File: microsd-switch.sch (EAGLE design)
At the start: 12 parts, among them IC1 SN74CBT3257D, IC2 SN74CBT3257D, U1 USD-SOCKETNEW

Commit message: Reduced uSD header connector size.
Signed-off-by: Joel Fernandes <joelf@ti.com>
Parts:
- JP2: value USD-HEADER-TARGET -> SD_HEADER_TARGET; device SparkFun:M08LOCK -> joels-parts:M08
- JP3: value USD-HEADER-HOST -> SD_HEADER_HOST; device SparkFun:M08LOCK -> joels-parts:M08
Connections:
- net CLK-A: now also JP2.6; no longer JP2.3
- net CLK-B: now also JP3.6; no longer JP3.3
- net CMD-A: now also JP2.3; no longer JP2.6
- net CMD-B: now also JP3.3; no longer JP3.6
- net DAT0-A: now also JP2.7; no longer JP2.2
- net DAT0-B: now also JP3.7; no longer JP3.2
- net DAT1-A: now also JP2.8; no longer JP2.1
- net DAT1-B: now also JP3.8; no longer JP3.1
- net DAT2-A: now also JP2.1; no longer JP2.8
- net DAT2-B: now also JP3.1; no longer JP3.8
- net DAT3-A: now also JP2.2; no longer JP2.7
- net DAT3-B: now also JP3.2; no longer JP3.7
- net GND: now also JP2.4, JP3.4; no longer JP2.5, JP3.5
- net VDD-A: now also JP2.5; no longer JP2.4
- net VDD-B: now also JP3.5; no longer JP3.4
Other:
- moved on the sheet: JP2, JP3
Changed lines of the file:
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@@
 <part name="GND2" library="supply1" deviceset="GND" device=""/>
 <part name="P+1" library="supply1" deviceset="VCC" device=""/>
-<part name="JP2" library="SparkFun" deviceset="M08" device="LOCK" value="USD-HEADER-TARGET"/>
-<part name="JP3" library="SparkFun" deviceset="M08" device="LOCK" value="USD-HEADER-HOST"/>
 <part name="IC1" library="joels-parts" deviceset="SN74CBT3257" device="D"/>
 <part name="IC2" library="joels-parts" deviceset="SN74CBT3257" device="D"/>
@@
 <part name="LED2" library="led" deviceset="LED" device="CHIP-LED0805" value="SWITCH"/>
 <part name="GND1" library="supply1" deviceset="GND" device=""/>
+<part name="JP2" library="joels-parts" deviceset="M08" device="" value="SD_HEADER_TARGET"/>
+<part name="JP3" library="joels-parts" deviceset="M08" device="" value="SD_HEADER_HOST"/>
 </parts>
 <sheets>
@@
 <instance part="GND2" gate="1" x="17.78" y="0"/>
 <instance part="P+1" gate="VCC" x="-15.24" y="2.54" rot="MR0"/>
-<instance part="JP2" gate="G$1" x="-7.62" y="71.12" rot="MR180"/>
-<instance part="JP3" gate="G$1" x="-7.62" y="35.56" rot="MR180"/>
 <instance part="IC1" gate="A" x="45.72" y="60.96"/>
 <instance part="IC2" gate="A" x="45.72" y="22.86"/>
@@
 <instance part="LED2" gate="G$1" x="43.18" y="-7.62" rot="R90"/>
 <instance part="GND1" gate="1" x="63.5" y="-12.7"/>
+<instance part="JP2" gate="G$1" x="-7.62" y="68.58"/>
+<instance part="JP3" gate="G$1" x="-7.62" y="33.02"/>
 </instances>
 <busses>
@@
 <wire x1="-2.54" y1="78.74" x2="12.7" y2="78.74" width="0.1524" layer="91"/>
 <label x="2.54" y="78.74" size="1.778" layer="95"/>
-<pinref part="JP2" gate="G$1" pin="1"/>
+<pinref part="JP2" gate="G$1" pin="8"/>
 </segment>
 <segment>
@@
 <wire x1="-2.54" y1="76.2" x2="12.7" y2="76.2" width="0.1524" layer="91"/>
 <label x="2.54" y="76.2" size="1.778" layer="95"/>
-<pinref part="JP2" gate="G$1" pin="2"/>
+<pinref part="JP2" gate="G$1" pin="7"/>
 </segment>
 <segment>
@@
 </segment>
 <segment>
-<pinref part="JP2" gate="G$1" pin="4"/>
 <wire x1="-2.54" y1="71.12" x2="12.7" y2="71.12" width="0.1524" layer="91"/>
 <label x="2.54" y="71.12" size="1.778" layer="95"/>
+<pinref part="JP2" gate="G$1" pin="5"/>
 </segment>
 </net>
@@
 </segment>
 <segment>
-<pinref part="JP2" gate="G$1" pin="6"/>
 <wire x1="-2.54" y1="66.04" x2="12.7" y2="66.04" width="0.1524" layer="91"/>
 <label x="2.54" y="66.04" size="1.778" layer="95"/>
+<pinref part="JP2" gate="G$1" pin="3"/>
 </segment>
 </net>
@@
 <wire x1="-2.54" y1="63.5" x2="12.7" y2="63.5" width="0.1524" layer="91"/>
 <label x="5.08" y="63.5" size="1.778" layer="95"/>
-<pinref part="JP2" gate="G$1" pin="7"/>
+<pinref part="JP2" gate="G$1" pin="2"/>
 </segment>
 <segment>
@@
 <wire x1="-2.54" y1="60.96" x2="12.7" y2="60.96" width="0.1524" layer="91"/>
 <label x="5.08" y="60.96" size="1.778" layer="95"/>
-<pinref part="JP2" gate="G$1" pin="8"/>
+<pinref part="JP2" gate="G$1" pin="1"/>
 </segment>
 <segment>
@@
 <wire x1="-2.54" y1="43.18" x2="7.62" y2="43.18" width="0.1524" layer="91"/>
 <label x="5.08" y="43.18" size="1.778" layer="95"/>
-<pinref part="JP3" gate="G$1" pin="1"/>
+<pinref part="JP3" gate="G$1" pin="8"/>
 </segment>
 <segment>
@@
 <wire x1="-2.54" y1="40.64" x2="7.62" y2="40.64" width="0.1524" layer="91"/>
 <label x="5.08" y="40.64" size="1.778" layer="95"/>
-<pinref part="JP3" gate="G$1" pin="2"/>
+<pinref part="JP3" gate="G$1" pin="7"/>
 </segment>
 <segment>
@@
 </segment>
 <segment>
-<pinref part="JP3" gate="G$1" pin="3"/>
 <wire x1="-2.54" y1="38.1" x2="7.62" y2="38.1" width="0.1524" layer="91"/>
 <label x="5.08" y="38.1" size="1.778" layer="95"/>
+<pinref part="JP3" gate="G$1" pin="6"/>
 </segment>
 </net>
@@
 </segment>
 <segment>
-<pinref part="JP3" gate="G$1" pin="6"/>
 <wire x1="-2.54" y1="30.48" x2="7.62" y2="30.48" width="0.1524" layer="91"/>
 <label x="5.08" y="30.48" size="1.778" layer="95"/>
+<pinref part="JP3" gate="G$1" pin="3"/>
 </segment>
 </net>
@@
 <wire x1="-2.54" y1="27.94" x2="7.62" y2="27.94" width="0.1524" layer="91"/>
 <label x="5.08" y="27.94" size="1.778" layer="95"/>
-<pinref part="JP3" gate="G$1" pin="7"/>
+<pinref part="JP3" gate="G$1" pin="2"/>
 </segment>
 <segment>
@@
 <wire x1="-2.54" y1="25.4" x2="7.62" y2="25.4" width="0.1524" layer="91"/>
 <label x="5.08" y="25.4" size="1.778" layer="95"/>
-<pinref part="JP3" gate="G$1" pin="8"/>
+<pinref part="JP3" gate="G$1" pin="1"/>
 </segment>
 <segment>
@@
 </segment>
 <segment>
-<pinref part="JP3" gate="G$1" pin="4"/>
 <wire x1="-2.54" y1="35.56" x2="7.62" y2="35.56" width="0.1524" layer="91"/>
 <label x="5.08" y="35.56" size="1.778" layer="95"/>
+<pinref part="JP3" gate="G$1" pin="5"/>
 </segment>
 </net>
@@
 </segment>
 <segment>
-<pinref part="JP3" gate="G$1" pin="5"/>
 <wire x1="-2.54" y1="33.02" x2="7.62" y2="33.02" width="0.1524" layer="91"/>
 <label x="5.08" y="33.02" size="1.778" layer="95"/>
-</segment>
-<segment>
-<pinref part="JP2" gate="G$1" pin="5"/>
+<pinref part="JP3" gate="G$1" pin="4"/>
+</segment>
+<segment>
 <wire x1="-2.54" y1="68.58" x2="12.7" y2="68.58" width="0.1524" layer="91"/>
 <label x="2.54" y="68.58" size="1.778" layer="95"/>
+<pinref part="JP2" gate="G$1" pin="4"/>
 </segment>
 <segment>
@@
 </segment>
 <segment>
-<pinref part="JP2" gate="G$1" pin="3"/>
 <wire x1="-2.54" y1="73.66" x2="12.7" y2="73.66" width="0.1524" layer="91"/>
 <label x="2.54" y="73.66" size="1.778" layer="95"/>
-</segment>
-</net>
+<pinref part="JP2" gate="G$1" pin="6"/>
+</segment>
+</net>

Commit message: Revert "Reduced uSD header connector size."
This reverts commit 164ab6429ac06b889099512f0f315f421e6ea5d6.
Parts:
- JP2: value SD_HEADER_TARGET -> USD-HEADER-TARGET; device joels-parts:M08 -> SparkFun:M08LOCK
- JP3: value SD_HEADER_HOST -> USD-HEADER-HOST; device joels-parts:M08 -> SparkFun:M08LOCK
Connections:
- net CLK-A: now also JP2.3; no longer JP2.6
- net CLK-B: now also JP3.3; no longer JP3.6
- net CMD-A: now also JP2.6; no longer JP2.3
- net CMD-B: now also JP3.6; no longer JP3.3
- net DAT0-A: now also JP2.2; no longer JP2.7
- net DAT0-B: now also JP3.2; no longer JP3.7
- net DAT1-A: now also JP2.1; no longer JP2.8
- net DAT1-B: now also JP3.1; no longer JP3.8
- net DAT2-A: now also JP2.8; no longer JP2.1
- net DAT2-B: now also JP3.8; no longer JP3.1
- net DAT3-A: now also JP2.7; no longer JP2.2
- net DAT3-B: now also JP3.7; no longer JP3.2
- net GND: now also JP2.5, JP3.5; no longer JP2.4, JP3.4
- net VDD-A: now also JP2.4; no longer JP2.5
- net VDD-B: now also JP3.4; no longer JP3.5
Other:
- moved on the sheet: JP2, JP3
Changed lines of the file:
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@@
 <part name="GND2" library="supply1" deviceset="GND" device=""/>
 <part name="P+1" library="supply1" deviceset="VCC" device=""/>
+<part name="JP2" library="SparkFun" deviceset="M08" device="LOCK" value="USD-HEADER-TARGET"/>
+<part name="JP3" library="SparkFun" deviceset="M08" device="LOCK" value="USD-HEADER-HOST"/>
 <part name="IC1" library="joels-parts" deviceset="SN74CBT3257" device="D"/>
 <part name="IC2" library="joels-parts" deviceset="SN74CBT3257" device="D"/>
@@
 <part name="LED2" library="led" deviceset="LED" device="CHIP-LED0805" value="SWITCH"/>
 <part name="GND1" library="supply1" deviceset="GND" device=""/>
-<part name="JP2" library="joels-parts" deviceset="M08" device="" value="SD_HEADER_TARGET"/>
-<part name="JP3" library="joels-parts" deviceset="M08" device="" value="SD_HEADER_HOST"/>
 </parts>
 <sheets>
@@
 <instance part="GND2" gate="1" x="17.78" y="0"/>
 <instance part="P+1" gate="VCC" x="-15.24" y="2.54" rot="MR0"/>
+<instance part="JP2" gate="G$1" x="-7.62" y="71.12" rot="MR180"/>
+<instance part="JP3" gate="G$1" x="-7.62" y="35.56" rot="MR180"/>
 <instance part="IC1" gate="A" x="45.72" y="60.96"/>
 <instance part="IC2" gate="A" x="45.72" y="22.86"/>
@@
 <instance part="LED2" gate="G$1" x="43.18" y="-7.62" rot="R90"/>
 <instance part="GND1" gate="1" x="63.5" y="-12.7"/>
-<instance part="JP2" gate="G$1" x="-7.62" y="68.58"/>
-<instance part="JP3" gate="G$1" x="-7.62" y="33.02"/>
 </instances>
 <busses>
@@
 <wire x1="-2.54" y1="78.74" x2="12.7" y2="78.74" width="0.1524" layer="91"/>
 <label x="2.54" y="78.74" size="1.778" layer="95"/>
-<pinref part="JP2" gate="G$1" pin="8"/>
+<pinref part="JP2" gate="G$1" pin="1"/>
 </segment>
 <segment>
@@
 <wire x1="-2.54" y1="76.2" x2="12.7" y2="76.2" width="0.1524" layer="91"/>
 <label x="2.54" y="76.2" size="1.778" layer="95"/>
-<pinref part="JP2" gate="G$1" pin="7"/>
+<pinref part="JP2" gate="G$1" pin="2"/>
 </segment>
 <segment>
@@
 </segment>
 <segment>
+<pinref part="JP2" gate="G$1" pin="4"/>
 <wire x1="-2.54" y1="71.12" x2="12.7" y2="71.12" width="0.1524" layer="91"/>
 <label x="2.54" y="71.12" size="1.778" layer="95"/>
-<pinref part="JP2" gate="G$1" pin="5"/>
 </segment>
 </net>
@@
 </segment>
 <segment>
+<pinref part="JP2" gate="G$1" pin="6"/>
 <wire x1="-2.54" y1="66.04" x2="12.7" y2="66.04" width="0.1524" layer="91"/>
 <label x="2.54" y="66.04" size="1.778" layer="95"/>
-<pinref part="JP2" gate="G$1" pin="3"/>
 </segment>
 </net>
@@
 <wire x1="-2.54" y1="63.5" x2="12.7" y2="63.5" width="0.1524" layer="91"/>
 <label x="5.08" y="63.5" size="1.778" layer="95"/>
-<pinref part="JP2" gate="G$1" pin="2"/>
+<pinref part="JP2" gate="G$1" pin="7"/>
 </segment>
 <segment>
@@
 <wire x1="-2.54" y1="60.96" x2="12.7" y2="60.96" width="0.1524" layer="91"/>
 <label x="5.08" y="60.96" size="1.778" layer="95"/>
-<pinref part="JP2" gate="G$1" pin="1"/>
+<pinref part="JP2" gate="G$1" pin="8"/>
 </segment>
 <segment>
@@
 <wire x1="-2.54" y1="43.18" x2="7.62" y2="43.18" width="0.1524" layer="91"/>
 <label x="5.08" y="43.18" size="1.778" layer="95"/>
-<pinref part="JP3" gate="G$1" pin="8"/>
+<pinref part="JP3" gate="G$1" pin="1"/>
 </segment>
 <segment>
@@
 <wire x1="-2.54" y1="40.64" x2="7.62" y2="40.64" width="0.1524" layer="91"/>
 <label x="5.08" y="40.64" size="1.778" layer="95"/>
-<pinref part="JP3" gate="G$1" pin="7"/>
+<pinref part="JP3" gate="G$1" pin="2"/>
 </segment>
 <segment>
@@
 </segment>
 <segment>
+<pinref part="JP3" gate="G$1" pin="3"/>
 <wire x1="-2.54" y1="38.1" x2="7.62" y2="38.1" width="0.1524" layer="91"/>
 <label x="5.08" y="38.1" size="1.778" layer="95"/>
-<pinref part="JP3" gate="G$1" pin="6"/>
 </segment>
 </net>
@@
 </segment>
 <segment>
+<pinref part="JP3" gate="G$1" pin="6"/>
 <wire x1="-2.54" y1="30.48" x2="7.62" y2="30.48" width="0.1524" layer="91"/>
 <label x="5.08" y="30.48" size="1.778" layer="95"/>
-<pinref part="JP3" gate="G$1" pin="3"/>
 </segment>
 </net>
@@
 <wire x1="-2.54" y1="27.94" x2="7.62" y2="27.94" width="0.1524" layer="91"/>
 <label x="5.08" y="27.94" size="1.778" layer="95"/>
-<pinref part="JP3" gate="G$1" pin="2"/>
+<pinref part="JP3" gate="G$1" pin="7"/>
 </segment>
 <segment>
@@
 <wire x1="-2.54" y1="25.4" x2="7.62" y2="25.4" width="0.1524" layer="91"/>
 <label x="5.08" y="25.4" size="1.778" layer="95"/>
-<pinref part="JP3" gate="G$1" pin="1"/>
+<pinref part="JP3" gate="G$1" pin="8"/>
 </segment>
 <segment>
@@
 </segment>
 <segment>
+<pinref part="JP3" gate="G$1" pin="4"/>
 <wire x1="-2.54" y1="35.56" x2="7.62" y2="35.56" width="0.1524" layer="91"/>
 <label x="5.08" y="35.56" size="1.778" layer="95"/>
-<pinref part="JP3" gate="G$1" pin="5"/>
 </segment>
 </net>
@@
 </segment>
 <segment>
+<pinref part="JP3" gate="G$1" pin="5"/>
 <wire x1="-2.54" y1="33.02" x2="7.62" y2="33.02" width="0.1524" layer="91"/>
 <label x="5.08" y="33.02" size="1.778" layer="95"/>
-<pinref part="JP3" gate="G$1" pin="4"/>
-</segment>
-<segment>
+</segment>
+<segment>
+<pinref part="JP2" gate="G$1" pin="5"/>
 <wire x1="-2.54" y1="68.58" x2="12.7" y2="68.58" width="0.1524" layer="91"/>
 <label x="2.54" y="68.58" size="1.778" layer="95"/>
-<pinref part="JP2" gate="G$1" pin="4"/>
 </segment>
 <segment>
@@
 </segment>
 <segment>
+<pinref part="JP2" gate="G$1" pin="3"/>
 <wire x1="-2.54" y1="73.66" x2="12.7" y2="73.66" width="0.1524" layer="91"/>
 <label x="2.54" y="73.66" size="1.778" layer="95"/>
-<pinref part="JP2" gate="G$1" pin="6"/>
-</segment>
-</net>
+</segment>
+</net>

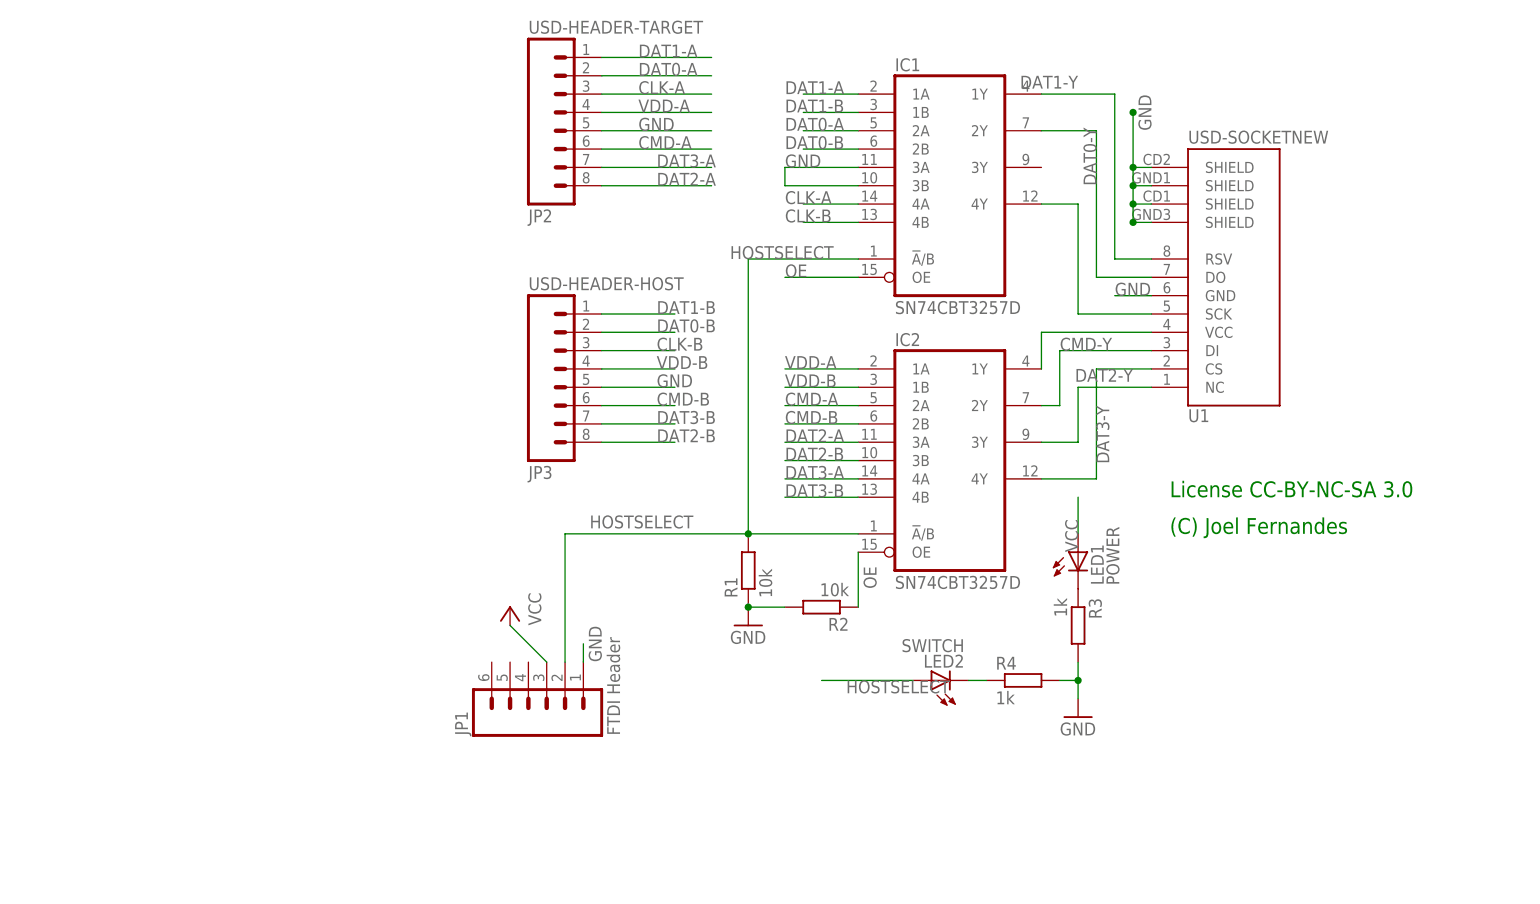
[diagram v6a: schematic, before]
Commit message: microsd-switch: Update board/schematic
Signed-off-by: Joel Fernandes <joelf@ti.com>
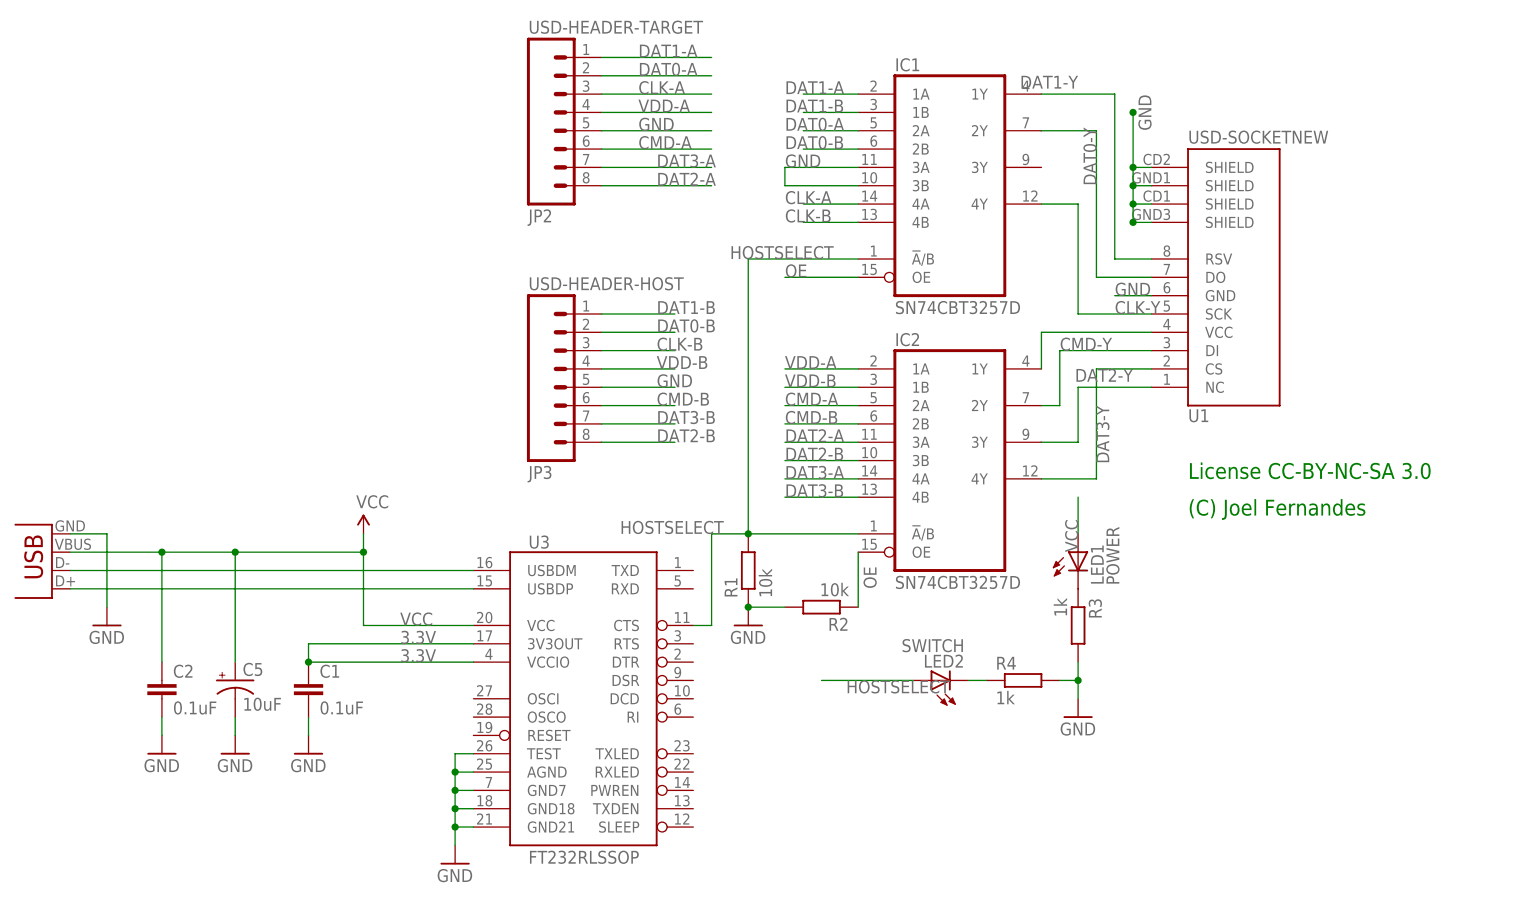
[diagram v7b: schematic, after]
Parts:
- removed JP1: FTDI Header, SparkFun:M06LOCK
- added C1, C2: 0.1uF, SparkFun:CAP0402-CAP
- added C5: 10uF, SparkFun:CAP_POL1206
- added U3: FT232RLSSOP, SparkFun:FT232RLSSOP
- added X2: USB-SMD-NS, SparkFun:USB-SMD-NS
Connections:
- net N$1 renamed CLK-Y
- new net 3.3V: C1.1, U3.3V3OUT, U3.VCCIO
- new net USB_D+: U3.USBDP, X2.D+
- new net USB_D-: U3.USBDM, X2.D-
- net GND: now also C1.2, C2.2, C5.-, U3.AGND, U3.GND18, U3.GND21, U3.GND7, U3.TEST, X2.GND; no longer JP1.1
- net HOSTSELECT: now also U3.CTS; no longer JP1.2
- net VCC: now also C2.1, C5.+, U3.VCC, X2.VBUS; no longer JP1.3
